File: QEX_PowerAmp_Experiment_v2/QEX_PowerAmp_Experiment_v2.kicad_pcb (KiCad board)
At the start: 4 copper layers, 87 x 74 mm, 73 parts, among them J1 Key In, J10 Conn_01x02, J11 SMA, J12 Conn_01x02, J2 Key In, J3 Conn_01x02, J4 Conn_01x02, J5 SMA, J6 Conn_01x02, J7 Conn_01x02, J8 Conn_01x03, J9 Conn_01x03, Q1 PZT2222A, Q2 DMN10H220LPDW, Q3 BC847BS, U1 74LVC2G125, U2 INA180A2, U3 MIC5205-3.3YM5, U5 UCC27517DBVR, U6 UCC27517DBVR, U7 LMR51430, U8 OPA1679

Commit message: Start version 2 of QEX amplifier
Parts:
- removed D2: 1N914A, Diode_THT:D_DO-35_SOD27_P7.62mm_Horizontal
- removed Q3: BC847BS, PCM_JLCPCB:SOT-363_SC-70-6
- removed R18: 0Ω, PCM_JLCPCB:R_0603
- removed R19: 30kΩ, PCM_JLCPCB:R_0603
- removed R20: 10kΩ, PCM_JLCPCB:R_0603
- removed TH1: Thermistor_NTC 10K, PCM_JLCPCB:R_0603
- added C22: 2.2uF, PCM_JLCPCB:C_0805, F.Cu at (63.8, 107.6)
- added C27: 4.7uF, PCM_JLCPCB:C_0805, F.Cu at (63.8, 110.7)
- added C28: 100nF, PCM_JLCPCB:C_0603, F.Cu at (57.5, 124.0)
- added C29: 100nF, PCM_JLCPCB:C_0603, F.Cu at (57.5, 126.2)
- added C30: 100nF, PCM_JLCPCB:C_0805, F.Cu at (63.8, 113.7)
- added C31: 22uF, PCM_JLCPCB:C_0805, F.Cu at (63.8, 116.8)
- added C32: 100nF, PCM_JLCPCB:C_0805, F.Cu at (63.8, 119.8)
- added C33: 22uF, PCM_JLCPCB:C_0805, F.Cu at (63.8, 122.9)
- added C34: 100uF, Capacitor_SMD:C_Elec_6.3x5.8, F.Cu at (71.0, 110.2)
- added C35: 314p, Capacitor_SMD:C_1206_3216Metric_Pad1.33x1.80mm_HandSolder, F.Cu at (58.6, 107.8)
- added C36: 44p, Capacitor_SMD:C_1206_3216Metric_Pad1.33x1.80mm_HandSolder, F.Cu at (58.6, 111.1)
- added C37: 609p, Capacitor_SMD:C_1206_3216Metric_Pad1.33x1.80mm_HandSolder, F.Cu at (58.6, 114.5)
- added C38: 101p, Capacitor_SMD:C_1206_3216Metric_Pad1.33x1.80mm_HandSolder, F.Cu at (58.6, 117.8)
- added C39: 279p, Capacitor_SMD:C_1206_3216Metric_Pad1.33x1.80mm_HandSolder, F.Cu at (58.6, 121.2)
- added J13: Conn_01x02, Connector_PinHeader_2.54mm:PinHeader_1x02_P2.54mm_Vertical, F.Cu at (72.7, 116.6)
- added J14: SMA, Connector_Coaxial:SMA_Molex_73251-1153_EdgeMount_Horizontal, F.Cu at (70.4, 88.4)
- added L4: L_Ferrite_Coupled, Transformer_THT:Transformer_Toroid_Horizontal_D14.0mm_Amidon-T50, F.Cu at (33.9, 123.6)
- added L5: 6.8uH, Inductor_THT:L_Toroid_Horizontal_D9.5mm_P15.00mm_Diameter10-5mm_Amidon-T37, F.Cu at (57.5, 100.6)
- added L6: 364n, Inductor_THT:L_Toroid_Horizontal_D12.7mm_P20.00mm_Diameter14-5mm_Amidon-T50, F.Cu at (33.6, 88.9)
- added L7: 311n, Inductor_THT:L_Toroid_Horizontal_D12.7mm_P20.00mm_Diameter14-5mm_Amidon-T50, F.Cu at (33.6, 103.2)
- added R8: 36kΩ, PCM_JLCPCB:R_0603, F.Cu at (63.4, 125.5)
- added TP1: VIN, TestPoint:TestPoint_Keystone_5000-5004_Miniature, F.Cu at (68.2, 116.4)
- added TP2: VBST, TestPoint:TestPoint_Keystone_5000-5004_Miniature, F.Cu at (68.2, 120.8)
- added TP3: VAMP, TestPoint:TestPoint_Keystone_5000-5004_Miniature, F.Cu at (68.2, 125.1)
- added U4: MIC5235-3.3YM5, Package_TO_SOT_SMD:SOT-23-5, F.Cu at (72.9, 123.8)
- C1: value 1uF -> 47uF; footprint PCM_JLCPCB:C_0603 -> Capacitor_SMD:CP_Elec_6.3x5.8
- C10: value 2.2uF -> 1uF; footprint PCM_JLCPCB:C_0805 -> Capacitor_SMD:C_0603_1608Metric_Pad1.08x0.95mm_HandSolder
- C12: value 220nF -> 100nF
- C13: value 22nF -> 220nF
- C14: value 100nF -> 22nF
- C15: value 100nF -> 4.7uF; footprint PCM_JLCPCB:C_0603 -> PCM_JLCPCB:C_0805
- C16: value 2.2uF -> 4.7uF
- C17, C7: value 2.2uF -> 100nF; footprint PCM_JLCPCB:C_0805 -> PCM_JLCPCB:C_0603
- C18, C19: value 4.7uF -> 100nF; footprint PCM_JLCPCB:C_0805 -> PCM_JLCPCB:C_0603
- C2, C3, C9: value 100nF -> 10uF; footprint PCM_JLCPCB:C_0603 -> Capacitor_SMD:C_1206_3216Metric_Pad1.33x1.80mm_HandSolder
- C21: value 100nF -> 2.2uF; footprint PCM_JLCPCB:C_0603 -> PCM_JLCPCB:C_0805
- C25: value 100uF -> 4.7uF; footprint Capacitor_SMD:C_Elec_6.3x5.8 -> PCM_JLCPCB:C_0805
- C26: value 100nF -> 100uF; footprint PCM_JLCPCB:C_0805 -> Capacitor_SMD:C_Elec_6.3x5.8
- C4: value 220nF -> 1uF; footprint PCM_JLCPCB:C_0603 -> Capacitor_SMD:C_0603_1608Metric_Pad1.08x0.95mm_HandSolder
- C5: value 1uF -> 220nF
- C8: value 1uF -> 10uF; footprint PCM_JLCPCB:C_0603 -> Capacitor_SMD:C_1206_3216Metric_Pad1.33x1.80mm_HandSolder
- D1: value 1N751A -> B240; footprint Diode_THT:D_DO-35_SOD27_P7.62mm_Horizontal -> Diode_SMD:D_SMB
- J1: value Key In -> Conn_01x02; footprint Connector_Coaxial:SMA_Molex_73251-1153_EdgeMount_Horizontal -> Connector_PinHeader_2.54mm:PinHeader_1x02_P2.54mm_Vertical
- J10, J3, J6: value Conn_01x02 -> Conn_01x03; footprint Connector_PinHeader_2.54mm:PinHeader_1x02_P2.54mm_Vertical -> Connector_PinHeader_2.54mm:PinHeader_1x03_P2.54mm_Vertical
- J11: value SMA -> Conn_01x03; footprint Connector_Coaxial:SMA_Molex_73251-1153_EdgeMount_Horizontal -> Connector_PinHeader_2.54mm:PinHeader_1x03_P2.54mm_Vertical
- J12: value Conn_01x02 -> SMA; footprint Connector_PinHeader_2.54mm:PinHeader_1x02_P2.54mm_Vertical -> Connector_Coaxial:SMA_Molex_73251-1153_EdgeMount_Horizontal
- J2: footprint Connector_PinHeader_2.54mm:PinHeader_1x02_P2.54mm_Vertical -> Connector_Coaxial:SMA_Molex_73251-1153_EdgeMount_Horizontal
- J4: value Conn_01x02 -> Key In
- J8: value Conn_01x03 -> Conn_01x02; footprint Connector_PinHeader_2.54mm:PinHeader_1x03_P2.54mm_Vertical -> Connector_PinHeader_2.54mm:PinHeader_1x02_P2.54mm_Vertical
- L1: value L_Ferrite_Coupled -> 4.7uH; footprint Transformer_THT:Transformer_Toroid_Horizontal_D14.0mm_Amidon-T50 -> Inductor_SMD:L_Coilcraft_XAL4030-XXX
- L2: value L_Ferrite_Coupled -> 6.8uH; footprint Transformer_THT:Transformer_Toroid_Horizontal_D14.0mm_Amidon-T50 -> Inductor_THT:L_Toroid_Horizontal_D9.5mm_P15.00mm_Diameter10-5mm_Amidon-T37
- L3: value 6.8uH -> L_Ferrite_Coupled; footprint Inductor_SMD:L_10.4x10.4_H4.8 -> Transformer_THT:Transformer_Toroid_Horizontal_D14.0mm_Amidon-T50
- Q1: value PZT2222A -> DMN10H220LPDW; footprint Package_TO_SOT_SMD:SOT-223 -> diodesInc:DMN10H220LPDW13
- Q2: value DMN10H220LPDW -> BC847BS; footprint diodesInc:DMN10H220LPDW13 -> PCM_JLCPCB:SOT-363_SC-70-6
- R11: value 0Ω -> 30kΩ
- R13: value 2.7kΩ -> 10kΩ
- R14: value 10kΩ -> 1kΩ
- R15: value 10kΩ -> 0Ω
- R16: value 10kΩ -> 30kΩ
- R17: value 0Ω -> 10kΩ
- R2: value 33kΩ -> 10kΩ
- R3: value 50m -> 33kΩ; footprint Resistor_SMD:R_0805_2012Metric_Pad1.20x1.40mm_HandSolder -> PCM_JLCPCB:R_0603
- R4: value 8.2kΩ -> 10kΩ
- R5: value 390 -> 100k; footprint Resistor_THT:R_Axial_DIN0207_L6.3mm_D2.5mm_P10.16mm_Horizontal -> Resistor_SMD:R_0603_1608Metric_Pad0.98x0.95mm_HandSolder
- R6: value 36kΩ -> 8.2kΩ
- R7: value 11kΩ -> 22k; footprint PCM_JLCPCB:R_0603 -> Resistor_SMD:R_0603_1608Metric_Pad0.98x0.95mm_HandSolder
- R9: value 10kΩ -> 11kΩ
- RV1: value 10K -> 5K
- U1: value 74LVC2G125 -> TLV61047DDC; footprint Package_SO:SSOP-8_2.95x2.8mm_P0.65mm -> Package_TO_SOT_SMD:SOT-23-5
- U2: value INA180A2 -> OPA1678; footprint Package_TO_SOT_SMD:SOT-23-5 -> Package_SO:SOIC-8_5.3x6.2mm_P1.27mm
- U3: value MIC5205-3.3YM5 -> 74LVC2G125; footprint Package_TO_SOT_SMD:SOT-23-5_HandSoldering -> Package_SO:SSOP-8_2.95x2.8mm_P0.65mm
- U5: value UCC27517DBVR -> LMR51430; footprint Package_TO_SOT_SMD:SOT-23-5_HandSoldering -> Package_TO_SOT_SMD:SOT-23-6
- U7: value LMR51430 -> UCC27517DBVR; footprint Package_TO_SOT_SMD:SOT-23-6 -> Package_TO_SOT_SMD:SOT-23-5_HandSoldering
- U8: value OPA1679 -> LMR51430; footprint Package_SO:SOIC-14_3.9x8.7mm_P1.27mm -> Package_TO_SOT_SMD:SOT-23-6
- moved C1 215.9 mm to (359.9, 71.9)
- moved C10 215.9 mm to (345.4, 99.9)
- moved C11 215.9 mm to (368.4, 67.4)
- moved C12 215.9 mm to (339.9, 65.4)
- moved C13 215.9 mm to (335.4, 65.4)
- moved C14 215.9 mm to (335.4, 111.4)
- moved C15 215.9 mm to (345.4, 104.9)
- moved C16 215.9 mm to (335.4, 113.9)
- moved C17 215.9 mm to (345.4, 102.4)
- moved C18 215.9 mm to (348.9, 79.9)
- moved C19 215.9 mm to (345.9, 79.9)
- moved C2 215.9 mm to (339.9, 118.4)
- moved C20 215.9 mm to (352.9, 80.9)
- moved C21 215.9 mm to (352.9, 87.4)
- moved C23 215.9 mm to (365.4, 90.9)
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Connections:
- C1 pad 1: /pwr-in -> /vin
- C10 pad 1: +5VA -> /vbst
- C11 pad 1: +5VA -> +3.3V
- C12 pad 1: /k4 -> +3.3V
- C12 pad 2: /k6 -> GND
- C13 pad 1: /k5 -> /k4
- C13 pad 2: GND -> /k6
- C14 pad 1: +5VA -> /k5
- C15 pad 1: +5VA -> VAMP
- C16 pad 1: +5VA -> VAMP
- C17 pad 1: +5VA -> VAMP
- C18 pad 1: +12VA -> +5VA
- C19 pad 1: +12VA -> Net-(U5-CB)
- C19 pad 2: GND -> /sw2
- C2 pad 1: +3.3V -> /vin
- C20 pad 1: +12VA -> +5VA
- C21 pad 1: Net-(U7-CB) -> +5VA
- C21 pad 2: /sw -> GND
- C23 pad 1: /VDD_AMP -> +5VA
- C24 pad 1: /VDD_AMP -> +5VA
- C25 pad 1: /VDD_AMP -> VAMP
- C26 pad 1: Net-(C26-Pad1) -> +5VA
- C3 pad 1: +3.3V -> /vin
- C4 pad 1: /k1 -> /vin
- C4 pad 2: /k3 -> GND
- C5 pad 1: +12VA -> /k1
- C5 pad 2: GND -> /k3
- C7 pad 1: Net-(U3-BP) -> VAMP
- C8 pad 1: /base -> /vbst
- C9 pad 1: +12VA -> /vbst
- D1 pad 1: /base -> /vbst
- J1 pad 1: /keyIn -> /vin
- J10 pad 1: /th_out -> /k6
- J10 pad 2: GND -> /k9
- J11 pad 1: /rf_out -> Net-(J11-Pin_1)
- J11 pad 2: GND -> Net-(J11-Pin_2)
- J12 pad 1: /VDD_AMP -> Net-(J11-Pin_3)
- J12 pad 2: /VDD_PWR -> GND
- J3 pad 1: /pwr-in -> /vin
- J3 pad 2: GND -> Net-(J3-Pin_2)
- J4 pad 1: /cs_out -> /keyIn
- J6 pad 1: /~{rf_enable} -> /vin
- J6 pad 2: GND -> VAMP
- J7 pad 1: /sw_enable -> /~{rf_enable}
- J8 pad 1: Net-(J8-Pin_1) -> /sw_enable
- J8 pad 2: /sw_enable -> GND
- J9 pad 1: /k8 -> Net-(J9-Pin_1)
- J9 pad 2: /k9 -> /sw_enable
- J9 pad 3: /k9 -> +3.3V
- L1 pad 1: /D2 -> /vin
- L1 pad 2: /D1 -> Net-(D1-A)
- L2 pad 1: /D1 -> /sw2
- L2 pad 2: /rf_out -> +5VA
- L3 pad 1: /sw -> /D2
- L3 pad 2: /VDD_AMP -> /D1
- Q1 pad 1: /base -> GND
- Q1 pad 2: +12VA -> /G2
- Q1 pad 3: +5VA -> GND
- Q1 pad 4: +12VA -> /G1
- Q2 pad 2: /G2 -> /cm1
- Q2 pad 3: GND -> /cm2
- Q2 pad 4: /G1 -> GND
- Q2 pad 5: /D1 -> /cm1
- Q2 pad 6: /D2 -> /cm1
- R1 pad 1: /keyIn -> Net-(J3-Pin_2)
- R10 pad 1: /k7 -> +3.3V
- R10 pad 2: GND -> /~{rf_enable}
- R11 pad 1: /k7 -> /fb2
- R11 pad 2: /k8 -> GND
- R12 pad 1: Net-(J8-Pin_3) -> Net-(J9-Pin_1)
- R12 pad 2: +3.3V -> GND
- R13 pad 1: /k9 -> /fb2
- R13 pad 2: /cm1 -> +5VA
- R14 pad 1: Net-(J8-Pin_1) -> /k9
- R14 pad 2: GND -> /cm1
- R15 pad 1: +3.3V -> /cm2
- R15 pad 2: /th1 -> /fb1
- R16 pad 1: Net-(U8D--) -> /fb1
- R17 pad 1: Net-(U8D--) -> /fb1
- R17 pad 2: /th_out -> /VDD_AMP
- R2 pad 2: /k1 -> GND
- R3 pad 1: /pwr-in -> /keyIn
- R3 pad 2: +12VA -> /k1
- R4 pad 1: /k1 -> Net-(U1-FB)
- R4 pad 2: /k2 -> GND
- R5 pad 1: +12VA -> Net-(U1-FB)
- R5 pad 2: /base -> Net-(R5-Pad2)
- R6 pad 1: /k3 -> /k1
- R6 pad 2: /k4 -> /k2
- R7 pad 1: /k4 -> Net-(R5-Pad2)
- R7 pad 2: /k5 -> /vbst
- R9 pad 1: +3.3V -> /k4
- R9 pad 2: /~{rf_enable} -> /k5
- RV1 pad 3: /k8 -> /k6
- U1 pad 1: /~{rf_enable} -> Net-(D1-A)
- U1 pad 2: /rfin -> GND
- U1 pad 3: /rfd+ -> Net-(U1-FB)
- U1 pad 4: GND -> Net-(J3-Pin_2)
- U1 pad 5: /rfin -> /vin
- U2 pad 1: /cs_out -> /k3
- U2 pad 2: GND -> /k3
- U2 pad 3: /pwr-in -> /k2
- U2 pad 4: +12VA -> GND
- U2 pad 5: +5VA -> /k5
- U3 pad 1: +5VA -> /~{rf_enable}
- U3 pad 2: GND -> /rfin
- U3 pad 3: +5VA -> /rfd+
- U3 pad 4: Net-(U3-BP) -> GND
- U3 pad 5: +3.3V -> /rfin
- U5 pad 1: +5VA -> GND
- U5 pad 2: GND -> /sw2
- U5 pad 3: /rfd+ -> VAMP
- U5 pad 4: GND -> /fb2
- U5 pad 5: /G1 -> /sw_enable
- U6 pad 3: +5VA -> /rfd+
- U6 pad 4: /rfd- -> GND
- U6 pad 5: /G2 -> /G1
- U7 pad 1: GND -> +5VA
- U7 pad 2: /sw -> GND
- U7 pad 3: +12VA -> +5VA
- U7 pad 4: /fb -> /rfd-
- U7 pad 5: /sw_enable -> /G2
- U8 pad 1: /k3 -> GND
- U8 pad 2: /k3 -> /sw1
- U8 pad 3: /k2 -> VAMP
- U8 pad 4: +12VA -> /fb1
- U8 pad 5: /k5 -> /sw_enable
- U8 pad 6: /k6 -> Net-(U8-CB)
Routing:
- net +5VA: track 103.8 -> 0.00 mm, vias 8 -> 0
- net +3.3V: track 94.8 -> 0.00 mm, vias 5 -> 0
- net /th1: track 85.5 -> 0.00 mm, vias 3 -> 0
- net GND: track 73.6 -> 0.00 mm, vias 111 -> 0
- net /sw_enable: track 60.8 -> 0.00 mm, vias 1 -> 0
- net /pwr-in: track 51.1 -> 0.00 mm
- net +12VA: track 41.3 -> 0.00 mm, vias 8 -> 0
- net /keyIn: track 34.3 -> 0.00 mm, vias 1 -> 0
- net /k8: track 33.6 -> 0.00 mm
- net /cs_out: track 31.6 -> 0.00 mm
- net /D2: track 30.1 -> 0.00 mm
- net /D1: track 29.7 -> 0.00 mm
- net /VDD_PWR: track 28.6 -> 0.00 mm
- net /~{rf_enable}: track 25.8 -> 0.00 mm
- net /k9: track 23.5 -> 0.00 mm
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- removed copper zone on In2.Cu, net +12VA
- removed copper zone on In2.Cu, net +5VA
- removed copper zone on F.Cu, net /VDD_AMP
- removed copper zone on F.Cu, net /sw
- removed copper zone on B.Cu, net GND
- removed copper zone on F.Cu, net GND
- removed copper zone on In1.Cu, net GND
- removed copper zone on In2.Cu, net GND
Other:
- board text removed: "+"
- board text removed: "Current Sense Output"
- board text removed: "Ext. Gain Control"
- board text removed: "Gain Control"
- board text removed: "Keyer Input"
- board text removed: "QRP Amplifier Test Board Version 1.0 N7WMN"
- board text removed: "RF Clock Input"
- board text removed: "RF Enable"
- board text removed: "RF Output"
- board text removed: "Supply Input 13.8V nominal"
- board text removed: "Switch Enable"
- board text removed: "Thermistor Output"
- board text removed: "gnd"
- board text removed: "jumper"

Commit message: Started layout of rev2 of QEX amplifier
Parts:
- removed J8: Conn_01x02, Connector_PinHeader_2.54mm:PinHeader_1x02_P2.54mm_Vertical
- removed R12: 10kΩ, PCM_JLCPCB:R_0603
- removed RV1: 5K, Potentiometer_THT:Potentiometer_Bourns_3296W_Vertical
- C35, C36, C37, C38, C39: moved to B.Cu
- J3: value Conn_01x03 -> Conn_01x02; footprint Connector_PinHeader_2.54mm:PinHeader_1x03_P2.54mm_Vertical -> Connector_PinHeader_2.54mm:PinHeader_1x02_P2.54mm_Vertical
- moved J4 281.9 mm to (106.0, 77.4), turned to 0 degrees
- moved J3 278.6 mm to (123.0, 83.0)
- moved J7 272.4 mm to (110.8, 126.0), turned to -90 degrees
- moved C11 253.1 mm to (119.2, 111.8), turned to 90 degrees
- moved C26 252.5 mm to (142.4, 101.1), turned to 0 degrees
- moved C1 250.8 mm to (109.5, 86.0), turned to 0 degrees
- moved R3 250.7 mm to (113.2, 65.2)
- moved C5 249.7 mm to (118.2, 66.0), turned to -90 degrees
- moved L2 243.6 mm to (132.0, 90.2)
- moved U2 241.9 mm to (122.0, 70.8)
- moved L1 240.1 mm to (118.0, 91.8)
- moved C20 237.9 mm to (118.0, 118.8), turned to 180 degrees
- moved R10 233.6 mm to (115.5, 111.8), turned to -90 degrees
- moved C12 233.4 mm to (114.0, 124.0), turned to 90 degrees
- moved C3 232.7 mm to (108.8, 93.2), turned to -90 degrees
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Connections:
- J9 pad 1: Net-(J9-Pin_1) -> GND

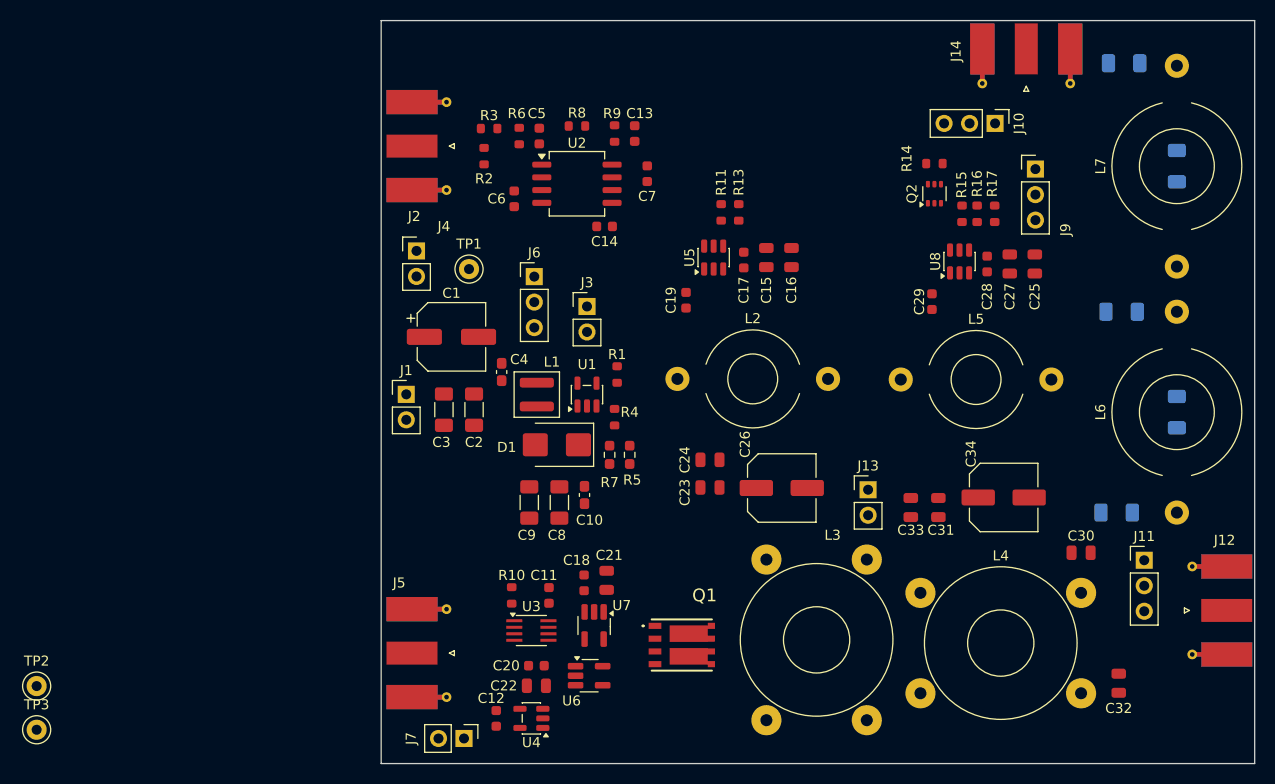
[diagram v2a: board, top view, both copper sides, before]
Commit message: Layout first pass with 0 unrouted.
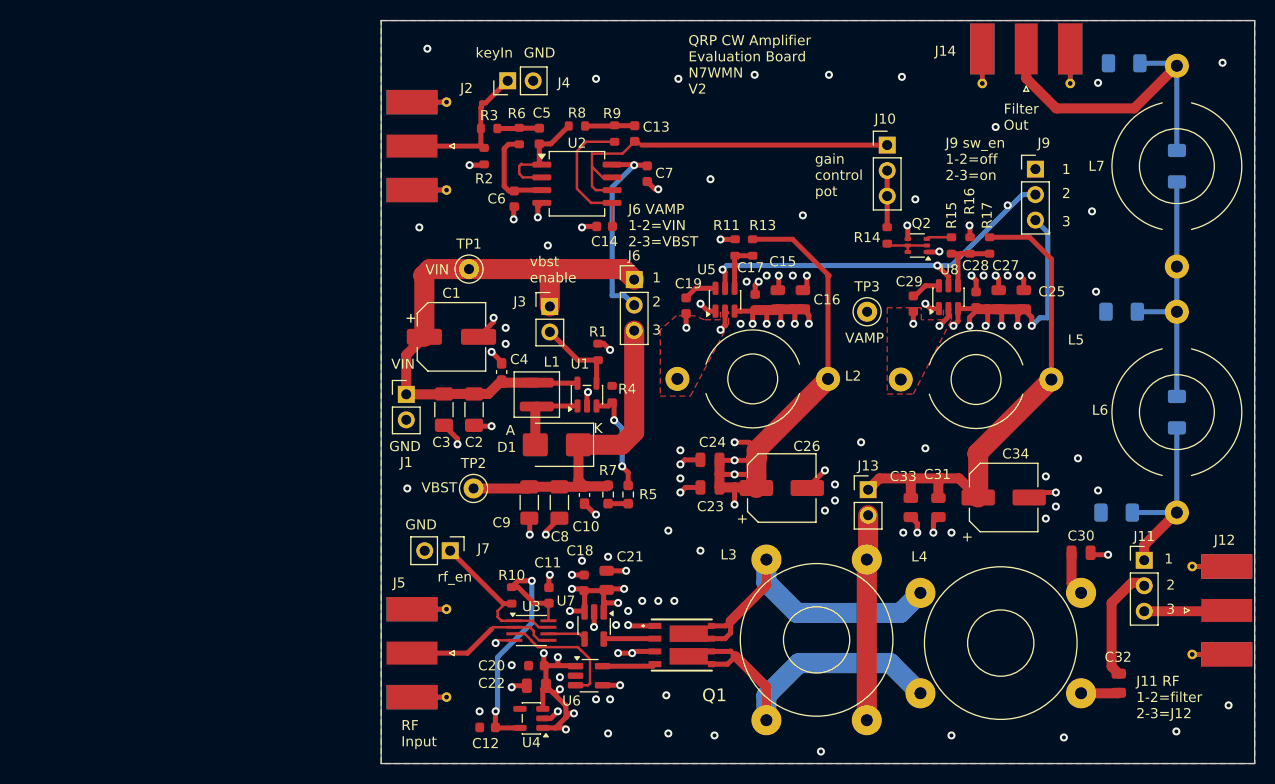
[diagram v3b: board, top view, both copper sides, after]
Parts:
- moved TP3 92.6 mm to (150.9, 83.5)
- moved TP2 47.8 mm to (111.7, 101.1)
- moved J4 19.2 mm to (115.1, 60.5), turned to 90 degrees
- moved J7 18.8 mm to (109.4, 107.3)
- moved J10 11.0 mm to (152.9, 66.9), turned to 0 degrees
- moved J6 9.95 mm to (127.7, 80.3)
- moved R14 8.57 mm to (152.9, 75.9), turned to -90 degrees
- moved Q2 5.43 mm to (155.9, 76.9), turned to 180 degrees
- moved C15 4.35 mm to (142.0, 82.3)
- moved C16 4.35 mm to (144.5, 82.3)
- moved C17 4.35 mm to (139.8, 82.5)
- moved U5 4.35 mm to (136.8, 82.3)
- moved R5 3.95 mm to (127.1, 101.7)
- moved R7 3.95 mm to (125.1, 101.7)
- moved R11 3.76 mm to (137.8, 77.1)
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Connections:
- J9 pad 3: +3.3V -> VAMP
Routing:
- net +5VA: track 0.00 -> 83.7 mm, vias 0 -> 13
- net GND: track 0.00 -> 76.8 mm, vias 0 -> 108
- net VAMP: track 0.00 -> 64.8 mm, vias 0 -> 13
- net /vin: track 0.00 -> 56.2 mm
- net /VDD_AMP: track 0.00 -> 50.1 mm
- net /sw_enable: track 0.00 -> 38.7 mm, vias 0 -> 2
- net /k6: track 0.00 -> 37.9 mm
- net /vbst: track 0.00 -> 34.1 mm
- net /D1: track 0.00 -> 33.4 mm
- net Net-(J14-In): track 0.00 -> 33.2 mm
- net /D2: track 0.00 -> 32.8 mm
- net +3.3V: track 0.00 -> 27.0 mm, vias 0 -> 2
- net Net-(C36-Pad2): track 0.00 -> 25.3 mm
- net /VDD_PWR: track 0.00 -> 20.5 mm
- net Net-(J11-Pin_1): track 0.00 -> 19.0 mm
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- added copper zone on In2.Cu, net +5VA
- added copper zone on F.Cu, net /sw1
- added copper zone on F.Cu, net /sw2
- added copper zone on In2.Cu, net /vin
- added copper zone on B.Cu, net GND
- added copper zone on F.Cu, net GND
- added copper zone on In1.Cu, net GND
- added copper zone on In2.Cu, net GND
- added copper zone on In2.Cu, net VAMP
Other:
- board text added: "+"
- board text added: "1"
- board text added: "2"
- board text added: "3"
- board text added: "A"
- board text added: "Filter Out"
- board text added: "GND"
- board text added: "J11 RF 1-2=filter 2-3=J12"
- board text added: "J6 VAMP 1-2=VIN 2-3=VBST"
- board text added: "J9 sw_en 1-2=off 2-3=on"
- board text added: "K"
- board text added: "QRP CW Amplifier Evaluation Board N7WMN V2"
- board text added: "RF Input"
- board text added: "VAMP"
- board text added: "VBST"
- board text added: "VIN"
- board text added: "gain control pot"
- board text added: "keyIn"
- board text added: "rf_en"
- board text added: "vbst enable"

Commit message: Layout cleanup and refining
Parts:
- removed R7: 22k, Resistor_SMD:R_0603_1608Metric_Pad0.98x0.95mm_HandSolder
- added C40: 47uF, Capacitor_SMD:CP_Elec_6.3x5.8, F.Cu at (162.3, 102.7)
- added C41: 10uF, Capacitor_SMD:C_1206_3216Metric_Pad1.33x1.80mm_HandSolder, F.Cu at (155.3, 102.9)
- added J8: Conn_01x03, Connector_PinHeader_2.54mm:PinHeader_1x03_P2.54mm_Vertical, F.Cu at (137.6, 71.7)
- C34: value 100uF -> 22uF; footprint Capacitor_SMD:C_Elec_6.3x5.8 -> PCM_JLCPCB:C_0805
- R5: value 100k -> 150K
- moved C33 22.2 mm to (173.9, 90.9), turned to 90 degrees
- moved C31 18.1 mm to (171.5, 90.9), turned to 90 degrees
- moved C34 12.0 mm to (169.1, 90.9), turned to 90 degrees
- moved L5 3.21 mm to (151.5, 91.9)
- moved C24 2.87 mm to (134.9, 101.1)
- moved C23 2.72 mm to (134.9, 103.7)
- moved C7 2.02 mm to (127.7, 71.3)
- moved L2 1.76 mm to (131.6, 91.9)
- moved C26 1.29 mm to (142.1, 102.3)
- moved R5 1.28 mm to (126.1, 100.9), turned to 180 degrees
- moved C15 1.00 mm to (142.0, 81.3)
- moved C16 1.00 mm to (144.5, 81.3)
- moved C17 1.00 mm to (139.8, 81.5)
- moved C19 1.00 mm to (132.9, 81.9)
- moved R11 1.00 mm to (137.8, 76.1)
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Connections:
- R5 pad 2: Net-(R5-Pad2) -> /vbst
- U5 pad 5: /sw_enable -> /sw2_en
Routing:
- net /sw_enable: track 38.7 -> 15.2 mm, vias 2 -> 1
- net /vin: track 56.2 -> 75.2 mm, vias 0 -> 8
- net VAMP: track 64.8 -> 83.4 mm, vias 13 -> 12
- net /sw2_en: track 0.00 -> 14.0 mm
- net /sw2: track 3.48 -> 15.6 mm, vias 2 -> 0
- net /sw1: track 3.31 -> 15.1 mm, vias 2 -> 0
- net +5VA: track 83.7 -> 72.3 mm, vias 13 -> 12
- net /VDD_PWR: track 20.5 -> 30.8 mm
- net Net-(R5-Pad2): track 2.00 -> 0.00 mm
- net GND: track 76.8 -> 75.4 mm, vias 108 -> 107
- net /VDD_AMP: track 50.1 -> 49.3 mm
- removed copper zone on F.Cu, net /sw1
- removed copper zone on F.Cu, net /sw2
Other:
- board text added: "J8 sw2_en 1-2=off 2-3=on"
- board text added: "Key Input"
- board text added: "QRP CW Amplifier Evaluation Board N7WMN V2.0"
- board text removed: "QRP CW Amplifier Evaluation Board N7WMN V2"

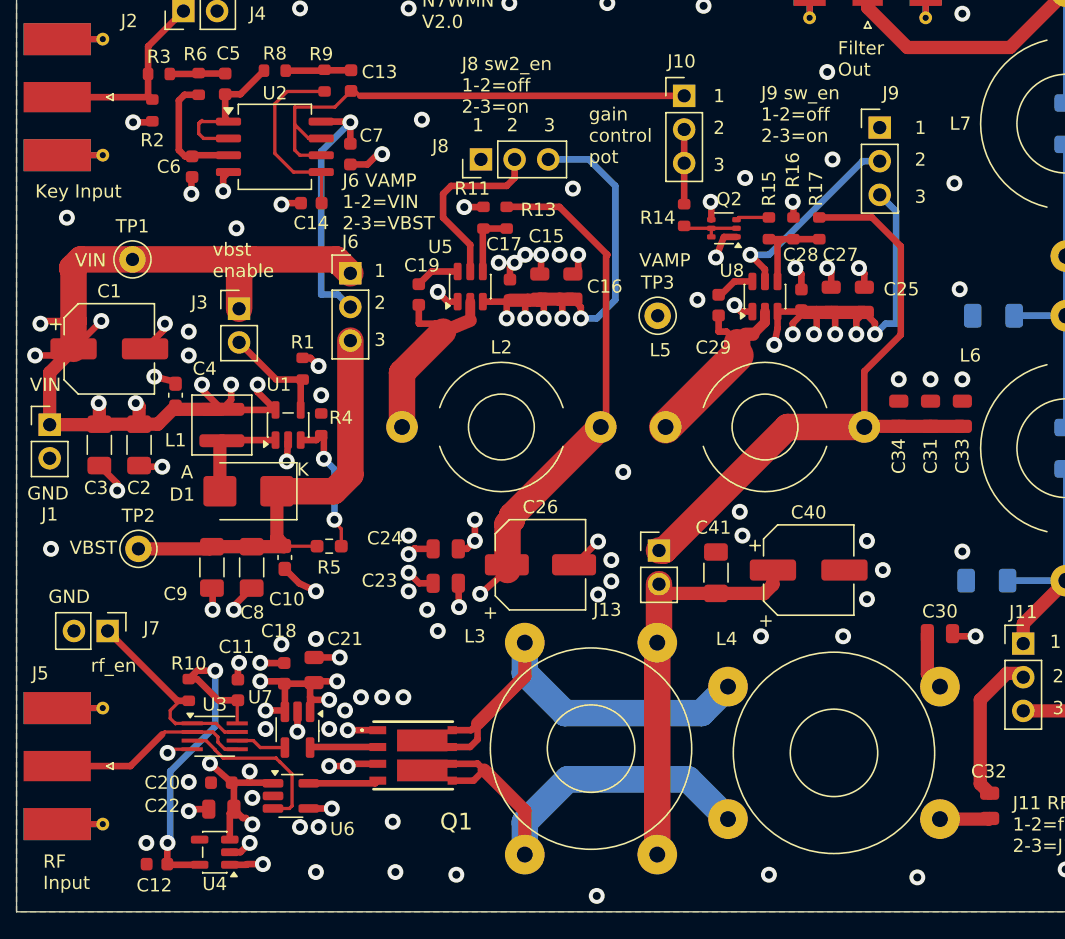
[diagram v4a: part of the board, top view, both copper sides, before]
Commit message: Taped Out package to JLCPCB
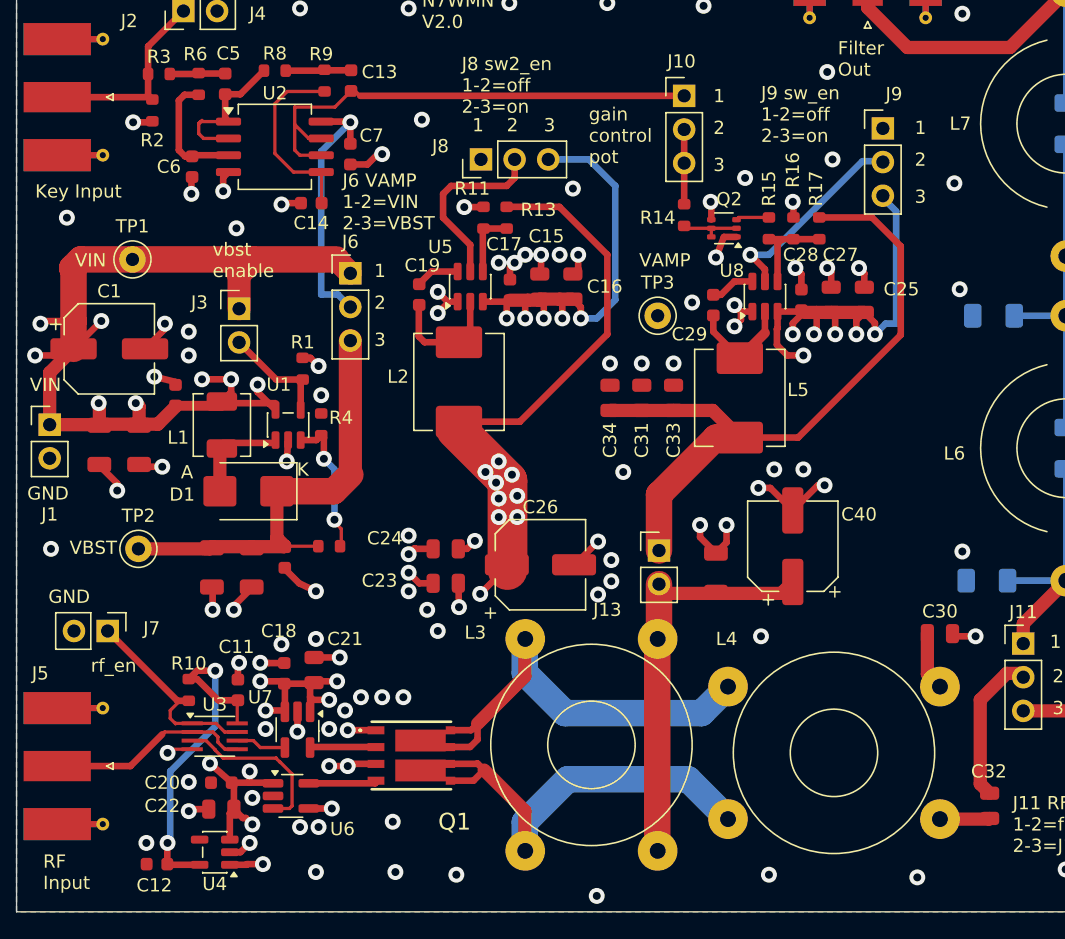
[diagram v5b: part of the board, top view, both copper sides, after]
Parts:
- C10, C4: footprint Capacitor_SMD:C_0603_1608Metric_Pad1.08x0.95mm_HandSolder -> PCM_JLCPCB:C_0603
- C2, C3, C41, C8, C9: footprint Capacitor_SMD:C_1206_3216Metric_Pad1.33x1.80mm_HandSolder -> PCM_JLCPCB:C_1206
- L1: footprint Inductor_SMD:L_Coilcraft_XAL4030-XXX -> Inductor_SMD:L_TechFuse_SL0420
- L2, L5: footprint Inductor_THT:L_Toroid_Horizontal_D9.5mm_P15.00mm_Diameter10-5mm_Amidon-T37 -> Inductor_SMD:L_TechFuse_SL0624
- R5: footprint Resistor_SMD:R_0603_1608Metric_Pad0.98x0.95mm_HandSolder -> PCM_JLCPCB:R_0603
- moved C31 21.8 mm to (149.7, 89.7)
- moved C33 21.8 mm to (152.1, 89.7)
- moved C34 21.8 mm to (147.3, 89.7)
- moved L5 6.02 mm to (157.1, 89.7), turned to -90 degrees
- moved L2 5.48 mm to (135.9, 88.5), turned to -90 degrees
- moved C40 2.16 mm to (161.1, 100.9), turned to 90 degrees
- moved C29 0.40 mm to (155.1, 82.7)
- moved L3 0.28 mm to (140.9, 107.9)
- moved J9 0.25 mm to (167.9, 69.4)
- moved Q1 0.14 mm to (134.9, 116.7)
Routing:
- net GND: track 75.4 -> 89.4 mm, vias 107 -> 109
- net /sw1: track 15.1 -> 8.35 mm
- net /sw2: track 15.6 -> 9.23 mm
- net +5VA: track 72.3 -> 76.0 mm, vias 12 -> 19
- net /VDD_AMP: track 49.3 -> 51.9 mm
- net VAMP: track 83.4 -> 85.7 mm
- net /vin: track 75.2 -> 74.4 mm
